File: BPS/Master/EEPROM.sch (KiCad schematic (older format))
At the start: 4 parts, among them U4 M24128

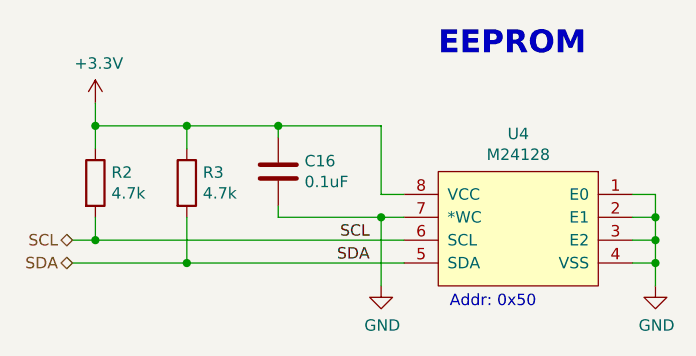
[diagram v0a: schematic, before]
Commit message: Creates fan brd interface schematics and updates symbols/footprints related to the leader board
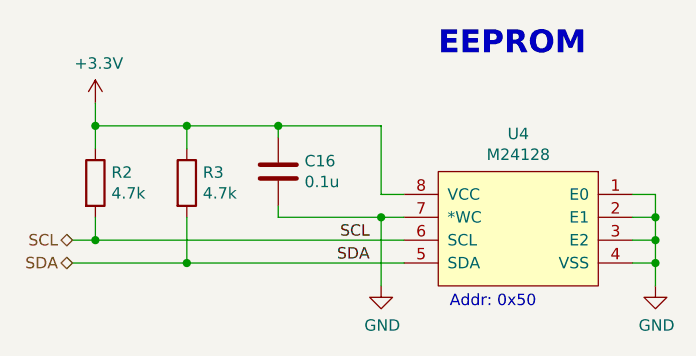
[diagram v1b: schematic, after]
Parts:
- removed U4: M24128, UTSVT_BPS:M24128-BRMN6P, symbol BPSMaster-rescue:M24128-utsvt-bps
- added U4: M24128, Package_SO:SOIC-8_3.9x4.9mm_P1.27mm, symbol utsvt-bps:M24128
- C16: value 0.1uF -> 0.1u
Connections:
- net +3V3: now also U4.8 (VCC)
- net GND: now also U4.1 (E0), U4.2 (E1), U4.3 (E2), U4.4 (VSS), U4.7 (*WC)
- net SCL: now also U4.6 (SCL)
- net SDA: now also U4.5 (SDA)
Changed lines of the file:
@@
 SCL
-$Comp
-L BPSMaster-rescue:M24128-utsvt-bps U4
-U 1 1 5C3511BE
-P 4250 2800
-F 0 "U4" H 4250 2965 50  0000 C CNN
-F 1 "M24128" H 4250 2874 50  0000 C CNN
-F 2 "UTSVT_BPS:M24128-BRMN6P" H 4250 2800 50  0001 C CNN
-F 3 "" H 4250 2800 50  0001 C CNN
-	1    4250 2800
-	-1   0    0    -1
-$EndComp
 $Comp
 L Device:C C16
@@
 P 3200 2800
 F 0 "C16" H 3315 2846 50  0000 L CNN
-F 1 "0.1uF" H 3315 2755 50  0000 L CNN
+F 1 "0.1u" H 3315 2755 50  0000 L CNN
 F 2 "Capacitor_SMD:C_0805_2012Metric" H 3238 2650 50  0001 C CNN
 F 3 "~" H 3200 2800 50  0001 C CNN
@@
 $EndComp
 $Comp
-L power:GND #PWR027
+L power:GND #PWR029
 U 1 1 5C3514DC
 P 4850 3300
-F 0 "#PWR027" H 4850 3050 50  0001 C CNN
+F 0 "#PWR029" H 4850 3050 50  0001 C CNN
 F 1 "GND" H 4855 3127 50  0000 C CNN
 F 2 "" H 4850 3300 50  0001 C CNN
@@
 Connection ~ 4850 3200
 $Comp
-L power:GND #PWR026
+L power:GND #PWR028
 U 1 1 5C3516F5
 P 3650 3300
-F 0 "#PWR026" H 3650 3050 50  0001 C CNN
+F 0 "#PWR028" H 3650 3050 50  0001 C CNN
 F 1 "GND" H 3655 3127 50  0000 C CNN
 F 2 "" H 3650 3300 50  0001 C CNN
@@
 $EndComp
 $Comp
-L power:+3.3V #PWR025
+L power:+3.3V #PWR027
 U 1 1 5C351A76
 P 2400 2500
-F 0 "#PWR025" H 2400 2350 50  0001 C CNN
+F 0 "#PWR027" H 2400 2350 50  0001 C CNN
 F 1 "+3.3V" H 2415 2673 50  0000 C CNN
 F 2 "" H 2400 2500 50  0001 C CNN
@@
 Wire Wire Line
 	2300 3200 2800 3200
+$Comp
+L utsvt-bps:M24128 U4
+U 1 1 5F1359C0
+P 4250 2800
+F 0 "U4" H 4250 2965 50  0000 C CNN
+F 1 "M24128" H 4250 2874 50  0000 C CNN
+F 2 "Package_SO:SOIC-8_3.9x4.9mm_P1.27mm" H 4250 2800 50  0001 C CNN
+F 3 "https://www.st.com/resource/en/datasheet/m24128-bf.pdf" H 4250 2800 50  0001 C CNN
+F 4 "0x50" H 4250 2800 50  0001 C CNN "Address"
+	1    4250 2800
+	-1   0    0    -1
+$EndComp
 $EndSCHEMATC
